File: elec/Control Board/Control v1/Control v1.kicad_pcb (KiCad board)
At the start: 2 copper layers, 126.3 x 160 mm, 185 parts, among them J1 DB9_Female_MountingHoles, J10 Conn_02x12_Odd_Even, J11 Screw_Terminal_01x02, J12 Screw_Terminal_01x02, J13 Screw_Terminal_01x02, J14 Conn_01x10, J15 DB25_Female_MountingHoles, J16 Conn_01x04, J17 Conn_01x05, J18 Conn_01x04, J19 Conn_01x07, J2 Conn_01x08, J20 Conn_01x04, J21 RJ12_6P6C_HORZ, J22 0.100_2Pin, J23 0.100_2Pin, J24 Conn_01x04, J3 Conn_01x08, J4 Conn_01x08, J5 Conn_01x08, J6 Conn_01x08, J7 Conn_01x10, J8 Conn_02x18_Odd_Even, J9 Conn_01x10, Q1 BSS138, Q10 BSS138, Q2 NCE01P30K, Q3 BSS138, Q4 BSS138, Q5 BSS138, Q6 BSS138, Q7 BSS138, Q8 BSS138, Q9 BSS138

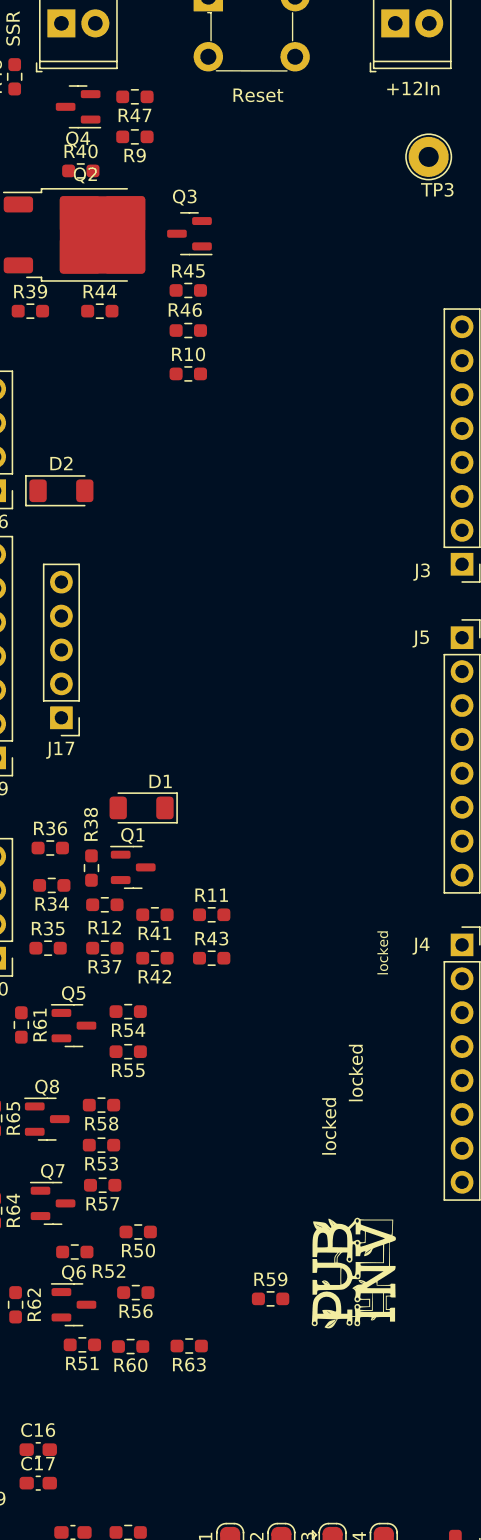
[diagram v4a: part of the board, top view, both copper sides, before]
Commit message: Add pull up to I2C. Add test points to SPI.
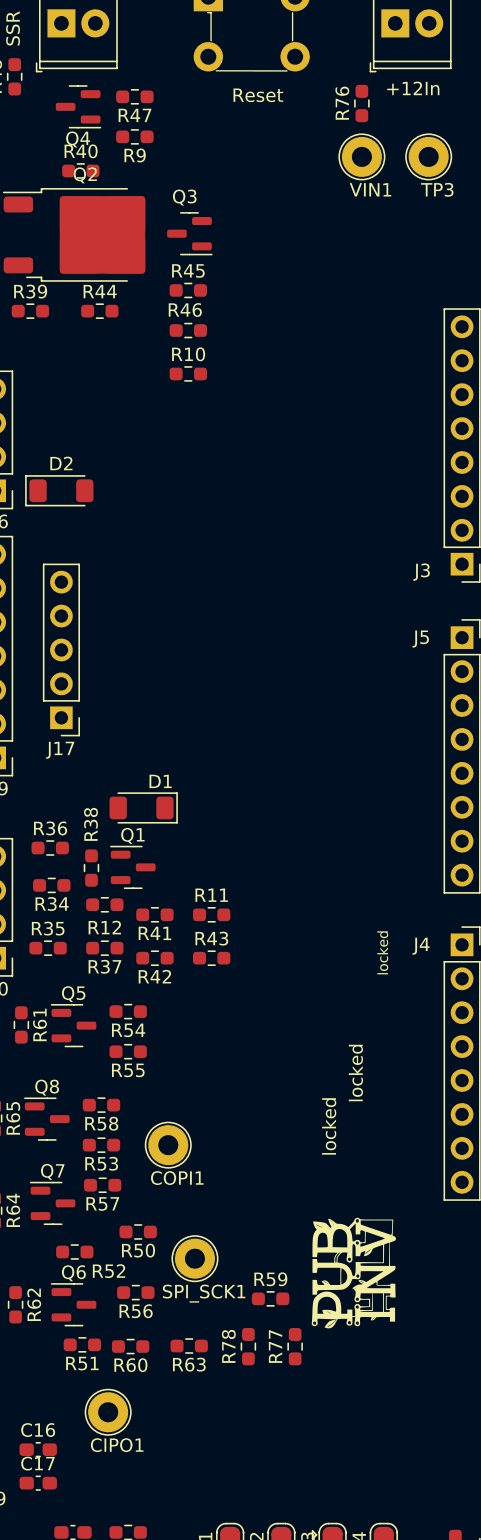
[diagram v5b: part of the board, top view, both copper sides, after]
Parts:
- added CIPO1: CIPO, TestPoint:TestPoint_Loop_D2.54mm_Drill1.5mm_Beaded, F.Cu at (78.5, 159.0)
- added COPI1: COPI, TestPoint:TestPoint_Loop_D2.54mm_Drill1.5mm_Beaded, F.Cu at (83.0, 139.0)
- added R76: 1R0, Resistor_SMD:R_0603_1608Metric_Pad0.98x0.95mm_HandSolder, F.Cu at (97.5, 61.0)
- added R77: 4K7, Resistor_SMD:R_0603_1608Metric_Pad0.98x0.95mm_HandSolder, F.Cu at (92.5, 154.1)
- added R78: 4K7, Resistor_SMD:R_0603_1608Metric_Pad0.98x0.95mm_HandSolder, F.Cu at (89.0, 154.1)
- added SPI_SCK1: SPI_SCK, TestPoint:TestPoint_Loop_D2.54mm_Drill1.5mm_Beaded, F.Cu at (85.0, 147.5)
- added VIN1: VIN1, TestPoint:TestPoint_Loop_D2.54mm_Drill1.5mm_Beaded, F.Cu at (97.5, 65.0)
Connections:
- net Net-(A1-SPI_RESET) renamed SPI_nRST
- net Net-(J10-Pin_19) renamed /PS_SCL
- net Net-(J10-Pin_20) renamed /PS_SDA
- A1 pad D24: Net-(J8-Pin_5) -> Net-(J8-Pin_6)
- A1 pad D26: Net-(J8-Pin_7) -> Net-(J8-Pin_8)
- A1 pad D28: Net-(J8-Pin_9) -> Net-(J8-Pin_10)
- A1 pad D30: Net-(J8-Pin_11) -> Net-(J8-Pin_12)
- A1 pad D33: D33 -> TC_nCS1
- A1 pad D34: D34 -> TC_nCS2
- A1 pad D35: D35 -> TC_nCS3
- A1 pad D36: Net-(J8-Pin_17) -> Net-(J8-Pin_18)
- A1 pad D38: Net-(J8-Pin_19) -> Net-(J8-Pin_20)
- A1 pad D40: Net-(J8-Pin_21) -> Net-(J8-Pin_22)
- A1 pad D42: Net-(J8-Pin_23) -> Net-(J8-Pin_24)
- A1 pad D44: Net-(J8-Pin_25) -> Net-(J8-Pin_26)
- A1 pad D46: Net-(J8-Pin_27) -> Net-(J8-Pin_28)
- A1 pad D48: Net-(J8-Pin_29) -> Net-(J8-Pin_30)
- A1 pad D50: Net-(J8-Pin_31) -> Net-(J8-Pin_32)
- A1 pad D53: Net-(J8-Pin_34) -> Net-(J8-Pin_33)
- A1 pad VIN: +12V -> Net-(J3-Pin_1)
- J3 pad 1: +12V -> Net-(J3-Pin_1)
- J8 pad 1: 5V3 -> 5V4
- J8 pad 10: D29 -> Net-(J8-Pin_10)
- J8 pad 11: Net-(J8-Pin_11) -> D31
- J8 pad 12: D31 -> Net-(J8-Pin_12)
- J8 pad 13: D32 -> TC_nCS1
- J8 pad 14: D33 -> D32
- J8 pad 15: D34 -> TC_nCS3
- J8 pad 16: D35 -> TC_nCS2
- J8 pad 17: Net-(J8-Pin_17) -> D37
- J8 pad 18: D37 -> Net-(J8-Pin_18)
- J8 pad 19: Net-(J8-Pin_19) -> D39
- J8 pad 2: 5V4 -> 5V3
- J8 pad 20: D39 -> Net-(J8-Pin_20)
- J8 pad 21: Net-(J8-Pin_21) -> D41
- J8 pad 22: D41 -> Net-(J8-Pin_22)
- J8 pad 23: Net-(J8-Pin_23) -> D43
- J8 pad 24: D43 -> Net-(J8-Pin_24)
- J8 pad 25: Net-(J8-Pin_25) -> D45
- J8 pad 26: D45 -> Net-(J8-Pin_26)
- J8 pad 27: Net-(J8-Pin_27) -> D47
- J8 pad 28: D47 -> Net-(J8-Pin_28)
- J8 pad 29: Net-(J8-Pin_29) -> D49
- J8 pad 3: BLOWER_ENABLE -> D23
- J8 pad 30: D49 -> Net-(J8-Pin_30)
- J8 pad 31: Net-(J8-Pin_31) -> D51
- J8 pad 32: D51 -> Net-(J8-Pin_32)
- J8 pad 33: Net-(A1-D52_CS2) -> Net-(J8-Pin_33)
- J8 pad 34: Net-(J8-Pin_34) -> Net-(A1-D52_CS2)
- J8 pad 4: D23 -> BLOWER_ENABLE
- J8 pad 5: Net-(J8-Pin_5) -> D25
- J8 pad 6: D25 -> Net-(J8-Pin_6)
- J8 pad 7: Net-(J8-Pin_7) -> D27
- J8 pad 8: D27 -> Net-(J8-Pin_8)
- J8 pad 9: Net-(J8-Pin_9) -> D29
- R1 pad 1: D35 -> TC_nCS3
- R3 pad 1: D34 -> TC_nCS2
- R7 pad 1: D33 -> TC_nCS1

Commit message: Changes during team review.
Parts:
- added C22: 10nF, Capacitor_SMD:C_0603_1608Metric_Pad1.08x0.95mm_HandSolder, F.Cu at (167.5, 59.5)
- added ISO1: MountingHole_Pad_3.5mm, PubInv_KiCad_PCB:MountingHole_3.5mm_Pad_Via, F.Cu at (63.5, 55.0)
- added ISO2: MountingHole_Pad_3.5mm, PubInv_KiCad_PCB:MountingHole_3.5mm_Pad_Via, F.Cu at (65.0, 205.0)
- added ISO3: MountingHole_Pad_3.5mm, PubInv_KiCad_PCB:MountingHole_3.5mm_Pad_Via, F.Cu at (172.0, 65.0)
- added ISO4: MountingHole_Pad_3.5mm, PubInv_KiCad_PCB:MountingHole_3.5mm_Pad_Via, F.Cu at (172.0, 195.0)
- added ISO5: MountingHole_Pad_3.5mm, PubInv_KiCad_PCB:MountingHole_3.5mm_Pad_Via, F.Cu at (172.0, 120.0)
- added J25: Screw_Terminal_01x02, TerminalBlock_TE-Connectivity:TerminalBlock_TE_282834-2_1x02_P2.54mm_Horizontal, F.Cu at (172.0, 185.2)
- added R79: 1R0, Resistor_SMD:R_0603_1608Metric_Pad0.98x0.95mm_HandSolder, F.Cu at (167.0, 185.0)
- added R80: 1R0, Resistor_SMD:R_0603_1608Metric_Pad0.98x0.95mm_HandSolder, F.Cu at (163.5, 185.0)
- added R81: 10K, Resistor_SMD:R_0603_1608Metric_Pad0.98x0.95mm_HandSolder, F.Cu at (84.5, 60.5)
- added R82: 1R0, Resistor_SMD:R_0603_1608Metric_Pad0.98x0.95mm_HandSolder, F.Cu at (161.0, 174.0)
- added R83: 4K7, Resistor_SMD:R_0603_1608Metric_Pad0.98x0.95mm_HandSolder, F.Cu at (103.0, 169.5)
- added R84: 1R0, Resistor_SMD:R_0603_1608Metric_Pad0.98x0.95mm_HandSolder, F.Cu at (106.2, 179.5)
- added R85: DNI, Resistor_SMD:R_0603_1608Metric_Pad0.98x0.95mm_HandSolder, F.Cu at (95.7, 160.5)
- added R86: DNI, Resistor_SMD:R_0603_1608Metric_Pad0.98x0.95mm_HandSolder, F.Cu at (95.7, 163.0)
- added R87: DNI, Resistor_SMD:R_0603_1608Metric_Pad0.98x0.95mm_HandSolder, F.Cu at (95.7, 165.5)
- added R88: 1R0, Resistor_SMD:R_0603_1608Metric_Pad0.98x0.95mm_HandSolder, F.Cu at (72.1, 63.0)
- added R89: DNI, Resistor_SMD:R_0603_1608Metric_Pad0.98x0.95mm_HandSolder, F.Cu at (84.5, 64.5)
- added R90: DNI, Resistor_SMD:R_0603_1608Metric_Pad0.98x0.95mm_HandSolder, F.Cu at (72.5, 76.5)
- R17, R30: value 1R0 -> DNI
- R32: value DNI -> 4M7
- moved R32 118.3 mm to (164.0, 59.5), turned to -90 degrees
- moved TP2 7.40 mm to (172.0, 109.5)
- moved TP10 6.90 mm to (163.0, 194.0)
- moved TP5 6.90 mm to (163.0, 205.6)
- moved TP9 6.90 mm to (163.0, 199.7)
- moved J12 6.23 mm to (70.2, 55.0)
- moved J13 5.00 mm to (80.0, 55.0)
- moved R39 2.96 mm to (72.5, 79.5)
- moved S1 2.76 mm to (88.8, 52.8)
- moved J11 1.73 mm to (101.7, 55.0)
- moved R1 1.50 mm to (106.0, 169.2)
- moved R48 1.50 mm to (71.5, 60.5), turned to 180 degrees
- moved JP10 0.72 mm to (127.7, 180.0)
- moved JP17 0.72 mm to (127.7, 188.0)
- moved JP20 0.72 mm to (130.7, 182.0)
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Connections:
- A1 pad D4: ONE_WIRE_TC -> Net-(A1-D4_CS1)
- A1 pad D5: Net-(J6-Pin_6) -> ONE_WIRE_TC
- J13 pad 1: +24V -> /SSR Interface/Heater_SSR_High
- J15 pad 14: /Blower controller/TachFan1 -> GND
- J15 pad 15: /Blower controller/TachFan1 -> GND
- J15 pad 16: /Blower controller/TachFan1 -> GND
- J15 pad 17: /Blower controller/TachFan1 -> GND
- J6 pad 5: ONE_WIRE_TC -> Net-(A1-D4_CS1)
- J6 pad 6: Net-(J6-Pin_6) -> ONE_WIRE_TC
- R32 pad 1: /Blower controller/TachFan1 -> GND
- R32 pad 2: GND -> Net-(C22-Pad2)

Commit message: Lots of routing. Lots remaining.
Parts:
- removed TP2: Due_5V2, TestPoint:TestPoint_Loop_D2.54mm_Drill1.5mm_Beaded
- added R91: 1R, Resistor_SMD:R_0603_1608Metric_Pad0.98x0.95mm_HandSolder, F.Cu at (104.1, 71.0)
- added R92: 1R, Resistor_SMD:R_0603_1608Metric_Pad0.98x0.95mm_HandSolder, F.Cu at (104.1, 73.5)
- moved C17 31.4 mm to (84.5, 135.0)
- moved R8 16.5 mm to (64.0, 167.0), turned to 0 degrees
- moved J19 15.6 mm to (79.5, 97.7)
- moved R39 14.3 mm to (69.5, 65.5)
- moved R44 11.9 mm to (73.5, 65.5)
- moved R33 9.64 mm to (69.5, 108.5)
- moved TP4 9.43 mm to (60.5, 60.0)
- moved R58 8.14 mm to (70.0, 134.5)
- moved SPI_SCK1 7.81 mm to (79.0, 142.5)
- moved TP18 7.07 mm to (67.0, 184.0)
- moved R59 6.65 mm to (84.5, 148.0), turned to 180 degrees
- moved R90 6.58 mm to (66.0, 77.5)
- moved R10 6.21 mm to (82.9, 75.2)
- moved R45 6.21 mm to (82.9, 69.0)
- moved R46 6.21 mm to (82.9, 72.0)
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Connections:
- net Net-(A1-D52_CS2) renamed D52
- net Net-(J15-P25) renamed /Blower controller/LOOPBACK25
- net Net-(J18-Pin_4) renamed /Blower controller/LOOPBACK13
- net Net-(J8-Pin_18) renamed LOOPBACK13
- net Net-(J8-Pin_22) renamed D40
- net Net-(J8-Pin_24) renamed D42
- net Net-(J8-Pin_26) renamed D44
- net Net-(J8-Pin_28) renamed D46
- net Net-(J8-Pin_30) renamed D48
- net Net-(J8-Pin_32) renamed D50
- net Net-(J8-Pin_33) renamed D53
- A1 pad 5V2: Net-(A1-SPI_5V) -> +5V
- A1 pad D38: Net-(J8-Pin_20) -> D38
- C1 pad 1: D35 -> D39
- J1 pad 1: D35 -> D39
- J8 pad 1: 5V4 -> +5V
- J8 pad 2: 5V3 -> +5V
- J8 pad 20: Net-(J8-Pin_20) -> D38
- R8 pad 2: D35 -> D38
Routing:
- net Net-(C22-Pad2): track 0.00 -> 373.7 mm, vias 0 -> 2
- net SPI_nRST: track 0.00 -> 99.6 mm, vias 0 -> 1
- net +5V: track 0.00 -> 82.3 mm, vias 0 -> 1
- net /Blower controller/TachFan1: track 0.00 -> 72.9 mm, vias 0 -> 1
- net /Blower controller/LOOPBACK25: track 0.00 -> 66.2 mm, vias 0 -> 1
- net /Blower controller/Switched_Fan_Power: track 0.00 -> 62.8 mm, vias 0 -> 3
- net /Blower controller/LOOPBACK13: track 0.00 -> 61.7 mm, vias 0 -> 1
- net /SPI_ControllerLevel_Shifter/CIPO: track 0.00 -> 51.1 mm
- net /SPI_ControllerLevel_Shifter/+5VLocal: track 0.00 -> 44.5 mm
- net Net-(J3-Pin_1): track 0.00 -> 44.1 mm, vias 0 -> 1
- net D39: track 0.00 -> 40.0 mm, vias 0 -> 1
- net +12V: track 0.00 -> 37.7 mm, vias 0 -> 1
- net /SSR Interface/Heater_SSR_High: track 0.00 -> 36.4 mm, vias 0 -> 2
- net /SPI_ControllerLevel_Shifter/COPI: track 0.00 -> 35.0 mm
- net /SPI_ControllerLevel_Shifter/C_SCK: track 0.00 -> 34.8 mm, vias 0 -> 1
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
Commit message: Lots of routing. Lots remaining.
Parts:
- moved R5 51.0 mm to (83.5, 162.5)
- moved R6 49.3 mm to (86.5, 162.5)
- moved R85 41.7 mm to (134.5, 176.0), turned to -90 degrees
- moved R2 30.1 mm to (159.5, 178.0)
- moved R3 19.5 mm to (129.5, 169.0)
- moved R16 18.9 mm to (168.0, 148.0), turned to -90 degrees
- moved R13 18.8 mm to (165.5, 148.0), turned to 90 degrees
- moved R86 17.2 mm to (108.5, 174.5), turned to -90 degrees
- moved R71 16.8 mm to (69.7, 194.8), turned to 0 degrees
- moved R87 16.3 mm to (82.5, 175.0), turned to -90 degrees
- moved R69 13.6 mm to (69.7, 191.8), turned to 0 degrees
- moved R68 10.0 mm to (70.4, 167.5), turned to 180 degrees
- moved TP6 9.66 mm to (141.0, 175.0)
- moved Q9 9.48 mm to (70.5, 187.8), turned to -90 degrees
- moved R31 9.19 mm to (160.0, 182.5)
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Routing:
- net +3.3V: track 6.21 -> 259.1 mm, vias 0 -> 4
- net SCL: track 9.88 -> 177.5 mm, vias 0 -> 4
- net /Thermocouple Amplifier with 1-Wire Breakout Board - MAX31850K/+VccMAX31850: track 0.00 -> 164.0 mm
- net SDA: track 9.84 -> 160.6 mm, vias 0 -> 7
- net BLOWER_ENABLE: track 11.9 -> 154.9 mm
- net D51: track 12.2 -> 154.9 mm, vias 0 -> 2
- net +12V: track 37.7 -> 173.8 mm, vias 1 -> 7
- net /Thermocouple Amplifier SPI Interface breakout board - MAX31855 /DO: track 0.00 -> 122.4 mm, vias 0 -> 6
- net /Thermocouple Amplifier SPI Interface breakout board - MAX31855 /+VccMAX31855: track 0.00 -> 117.3 mm
- net +5V: track 82.3 -> 189.2 mm, vias 1 -> 5
- net D37: track 12.1 -> 118.1 mm
- net LOOPBACK13: track 11.9 -> 113.2 mm
- net /Thermocouple Amplifier SPI Interface breakout board - MAX31855 /SCK: track 0.00 -> 94.7 mm, vias 0 -> 6
- net /I2C_LevelShift/+5VLocal: track 3.14 -> 54.2 mm, vias 0 -> 2
- net /Thermocouple Amplifier SPI Interface breakout board - MAX31855 /nCS_3: track 0.00 -> 35.7 mm
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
